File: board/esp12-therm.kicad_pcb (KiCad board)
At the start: 2 copper layers, 35.8 x 27.7 mm, 21 parts, among them J1 BATT, J2 I2C, J4 1W, Q1 IRLML6401, U1 TP4056_board, U2 ESP-12E

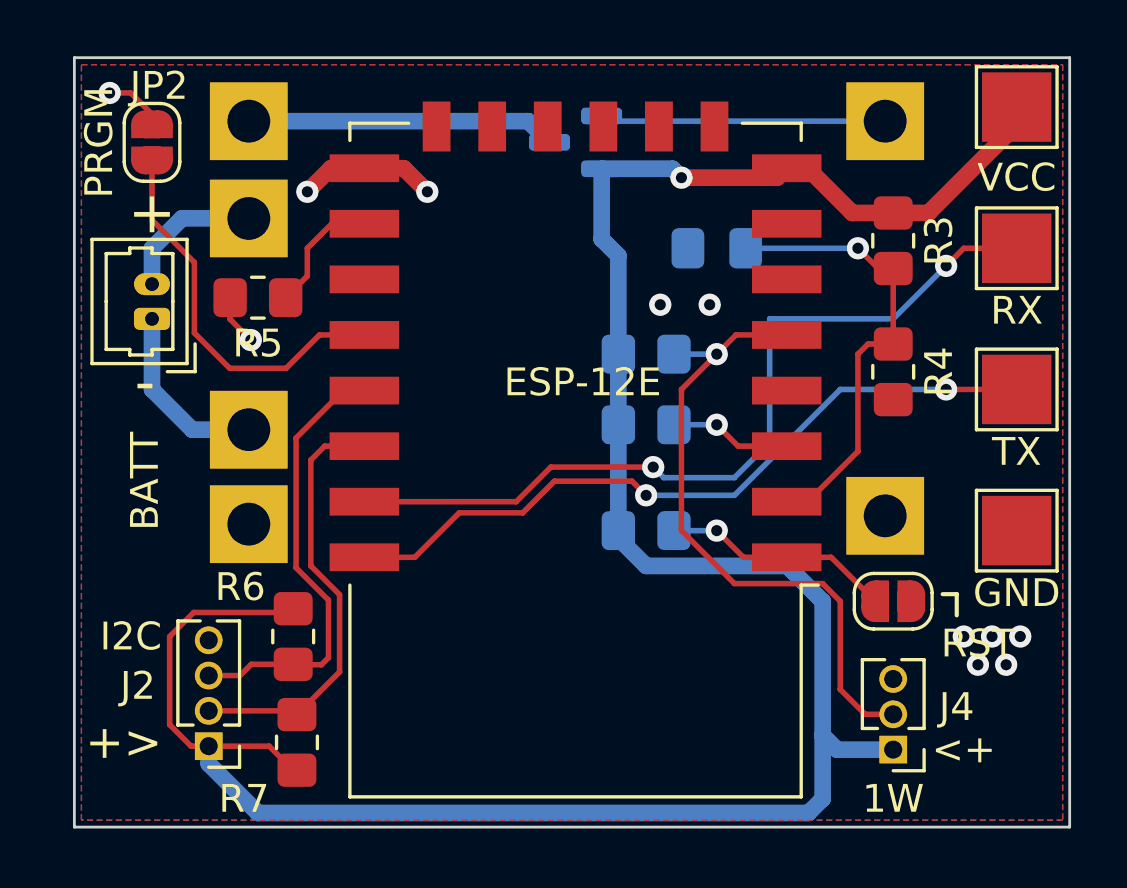
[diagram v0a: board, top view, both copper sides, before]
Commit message: Add JLC labels and silkscreen update, make board round
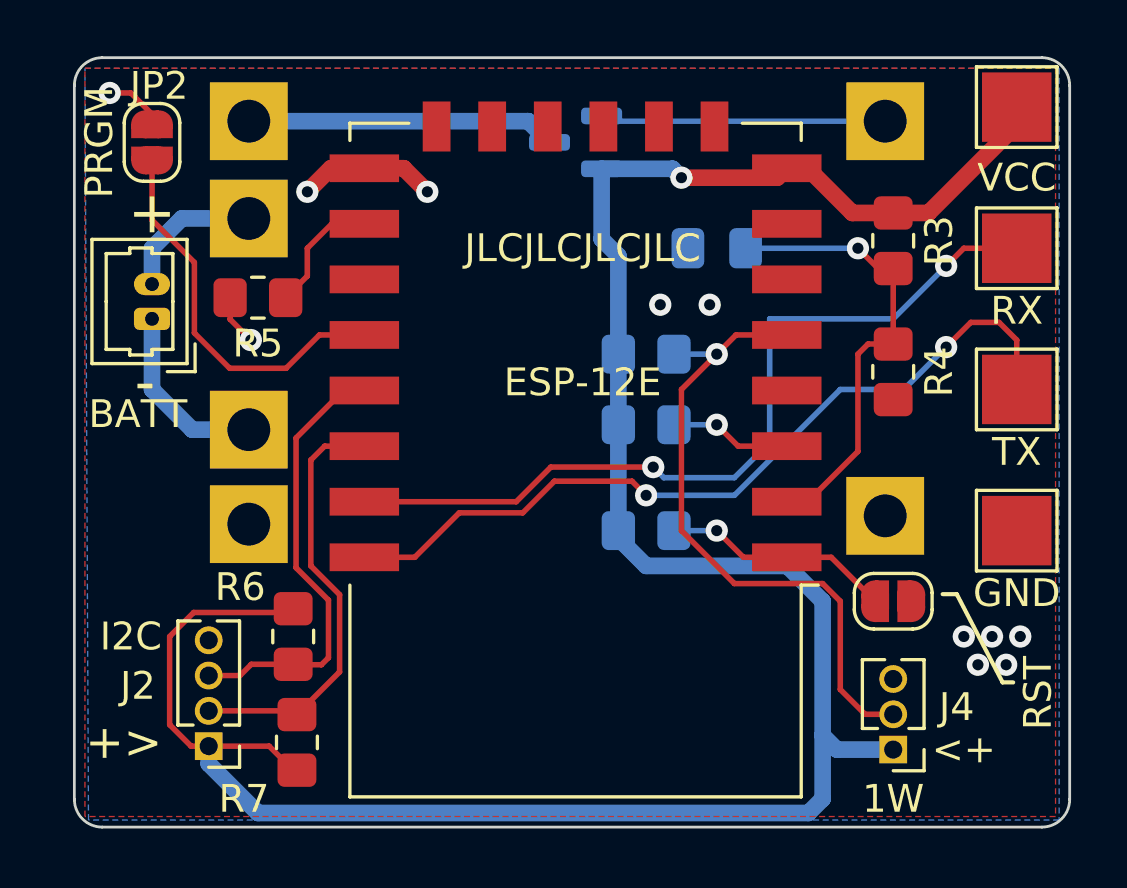
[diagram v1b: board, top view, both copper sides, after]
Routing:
- net TXD: track 26.4 -> 30.6 mm
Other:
- outline, holes or cut-outs redrawn
- board text added: "ESP12-thermometer (c) 2023"
- board text added: "JLCJLCJLCJLC"
- board text added: "https://gitlab.com/anphi/esp12-thermometer"

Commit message: Add Voltage regulator to board
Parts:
- added C2: 1u, Capacitor_SMD:C_0805_2012Metric_Pad1.18x1.45mm_HandSolder, B.Cu at (111.3, 59.2)
- added C3: 1u, Capacitor_SMD:C_0805_2012Metric_Pad1.18x1.45mm_HandSolder, B.Cu at (114.7, 60.1)
- added U3: TLV75533PDBV, Package_TO_SOT_SMD:SOT-23-5, B.Cu at (113.7, 56.3)
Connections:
- Q1 pad 2: VCC -> /VIN
- R3 pad 1: VCC -> /VIN
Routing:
- net /VIN: track 0.00 -> 37.0 mm, vias 0 -> 1
- net VCC: track 86.6 -> 90.3 mm
- net GND: track 9.06 -> 10.8 mm, vias 11 -> 10
- net RXD: track 30.2 -> 28.7 mm

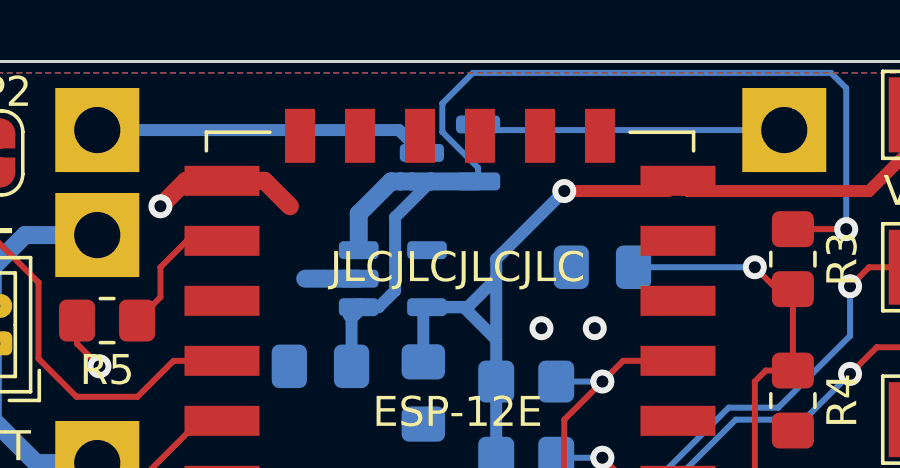
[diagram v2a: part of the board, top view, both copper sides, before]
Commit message: Change input MOSFET to an available one
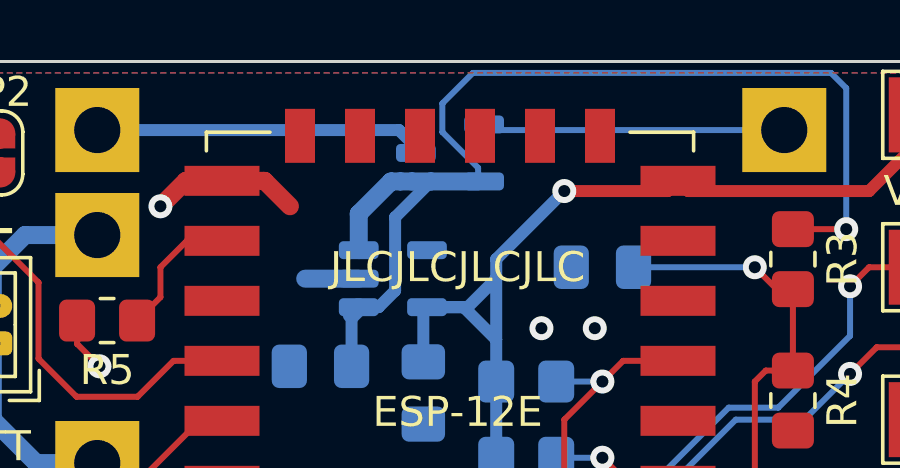
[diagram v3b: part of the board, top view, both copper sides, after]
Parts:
- Q1: value IRLML6401 -> PMF170XP; footprint Package_TO_SOT_SMD:SOT-23 -> Package_TO_SOT_SMD:SOT-23-3
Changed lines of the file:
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@@
       (net 3 "Net-(J1-Pin_1)") (pinfunction "B-") (pintype "power_out"))
   )
-  (footprint "Package_TO_SOT_SMD:SOT-23" (layer "B.Cu")
+  (footprint "Package_TO_SOT_SMD:SOT-23-3" (layer "B.Cu")
     (at 115.57 52.07 180)
-    (descr "SOT, 3 Pin (https://www.jedec.org/system/files/docs/to-236h.pdf variant AB), generated with kicad-footprint-generator ipc_gullwing_generator.py")
+    (descr "SOT, 3 Pin (https://www.jedec.org/sites/default/files/docs/Mo-178D.PDF inferred 3-pin variant), generated with kicad-footprint-generator ipc_gullwing_generator.py")
     (tags "SOT TO_SOT_SMD")
     (property "Sheetfile" "esp12-therm.kicad_sch")
@@
     (property "ki_keywords" "P-Channel HEXFET MOSFET Logic-Level")
     (attr smd)
-    (fp_text reference "Q1" (at 0 2.4) (layer "B.Fab")
+    (fp_text reference "Q1" (at 0 2.4) (layer "B.SilkS")
         (effects (font (size 1 1) (thickness 0.15)) (justify mirror))
     )
-    (fp_text value "IRLML6401" (at 0 -2.4) (layer "B.Fab")
+    (fp_text value "PMF170XP" (at 0 -2.4) (layer "B.Fab")
         (effects (font (size 1 1) (thickness 0.15)) (justify mirror))
     )
     (fp_text user "${REFERENCE}" (at 0 0) (layer "B.Fab")
-        (effects (font (size 0.32 0.32) (thickness 0.05)) (justify mirror))
+        (effects (font (size 0.4 0.4) (thickness 0.06)) (justify mirror))
     )
-    (fp_line (start 0 -1.56) (end -0.65 -1.56)
+    (fp_line (start 0 -1.56) (end -0.8 -1.56)
       (stroke (width 0.12) (type solid)) (layer "B.SilkS"))
-    (fp_line (start 0 -1.56) (end 0.65 -1.56)
+    (fp_line (start 0 -1.56) (end 0.8 -1.56)
       (stroke (width 0.12) (type solid)) (layer "B.SilkS"))
-    (fp_line (start 0 1.56) (end -1.675 1.56)
+    (fp_line (start 0 1.56) (end -1.8 1.56)
       (stroke (width 0.12) (type solid)) (layer "B.SilkS"))
-    (fp_line (start 0 1.56) (end 0.65 1.56)
+    (fp_line (start 0 1.56) (end 0.8 1.56)
       (stroke (width 0.12) (type solid)) (layer "B.SilkS"))
-    (fp_line (start -1.92 -1.7) (end 1.92 -1.7)
+    (fp_line (start -2.05 -1.7) (end 2.05 -1.7)
       (stroke (width 0.05) (type solid)) (layer "B.CrtYd"))
-    (fp_line (start -1.92 1.7) (end -1.92 -1.7)
+    (fp_line (start -2.05 1.7) (end -2.05 -1.7)
       (stroke (width 0.05) (type solid)) (layer "B.CrtYd"))
-    (fp_line (start 1.92 -1.7) (end 1.92 1.7)
+    (fp_line (start 2.05 -1.7) (end 2.05 1.7)
       (stroke (width 0.05) (type solid)) (layer "B.CrtYd"))
-    (fp_line (start 1.92 1.7) (end -1.92 1.7)
+    (fp_line (start 2.05 1.7) (end -2.05 1.7)
       (stroke (width 0.05) (type solid)) (layer "B.CrtYd"))
-    (fp_line (start -0.65 -1.45) (end -0.65 1.125)
+    (fp_line (start -0.8 -1.45) (end -0.8 1.05)
       (stroke (width 0.1) (type solid)) (layer "B.Fab"))
-    (fp_line (start -0.65 1.125) (end -0.325 1.45)
+    (fp_line (start -0.8 1.05) (end -0.4 1.45)
       (stroke (width 0.1) (type solid)) (layer "B.Fab"))
-    (fp_line (start -0.325 1.45) (end 0.65 1.45)
+    (fp_line (start -0.4 1.45) (end 0.8 1.45)
       (stroke (width 0.1) (type solid)) (layer "B.Fab"))
-    (fp_line (start 0.65 -1.45) (end -0.65 -1.45)
+    (fp_line (start 0.8 -1.45) (end -0.8 -1.45)
       (stroke (width 0.1) (type solid)) (layer "B.Fab"))
-    (fp_line (start 0.65 1.45) (end 0.65 -1.45)
+    (fp_line (start 0.8 1.45) (end 0.8 -1.45)
       (stroke (width 0.1) (type solid)) (layer "B.Fab"))
-    (pad "1" smd roundrect (at -0.9375 0.95 180) (size 1.475 0.6) (layers "B.Cu" "B.Paste" "B.Mask") (roundrect_rratio 0.25)
+    (pad "1" smd roundrect (at -1.1375 0.95 180) (size 1.325 0.6) (layers "B.Cu" "B.Paste" "B.Mask") (roundrect_rratio 0.25)
       (net 11 "Net-(Q1-G)") (pinfunction "G") (pintype "input"))
-    (pad "2" smd roundrect (at -0.9375 -0.95 180) (size 1.475 0.6) (layers "B.Cu" "B.Paste" "B.Mask") (roundrect_rratio 0.25)
+    (pad "2" smd roundrect (at -1.1375 -0.95 180) (size 1.325 0.6) (layers "B.Cu" "B.Paste" "B.Mask") (roundrect_rratio 0.25)
       (net 29 "/VIN") (pinfunction "S") (pintype "passive"))
-    (pad "3" smd roundrect (at 0.9375 0 180) (size 1.475 0.6) (layers "B.Cu" "B.Paste" "B.Mask") (roundrect_rratio 0.25)
+    (pad "3" smd roundrect (at 1.1375 0 180) (size 1.325 0.6) (layers "B.Cu" "B.Paste" "B.Mask") (roundrect_rratio 0.25)
       (net 12 "Net-(Q1-D)") (pinfunction "D") (pintype "passive"))
-    (model "${KICAD6_3DMODEL_DIR}/Package_TO_SOT_SMD.3dshapes/SOT-23.wrl"
+    (model "${KICAD6_3DMODEL_DIR}/Package_TO_SOT_SMD.3dshapes/SOT-23-3.wrl"
       (offset (xyz 0 0 0))
       (scale (xyz 1 1 1))

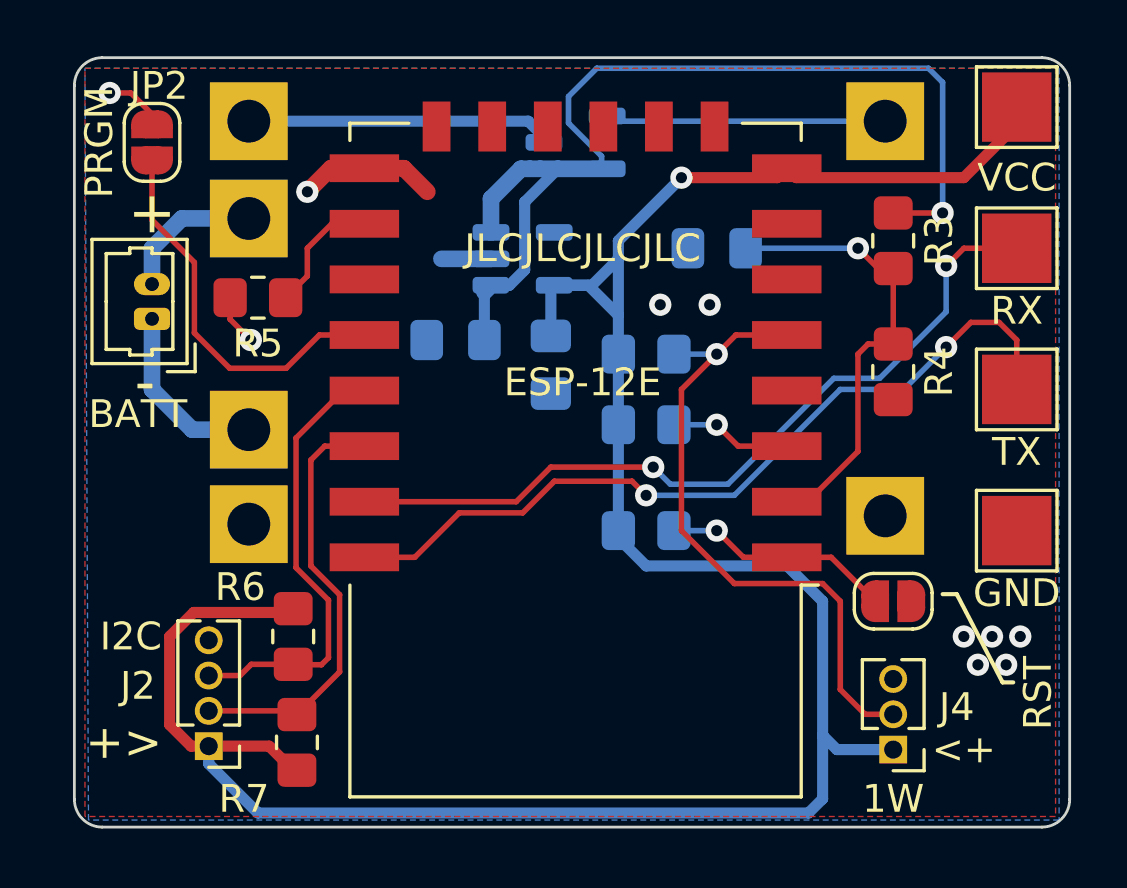
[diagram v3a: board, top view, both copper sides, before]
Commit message: * Adapt footprints to new MOSFET * Place battery bypass solder jumper
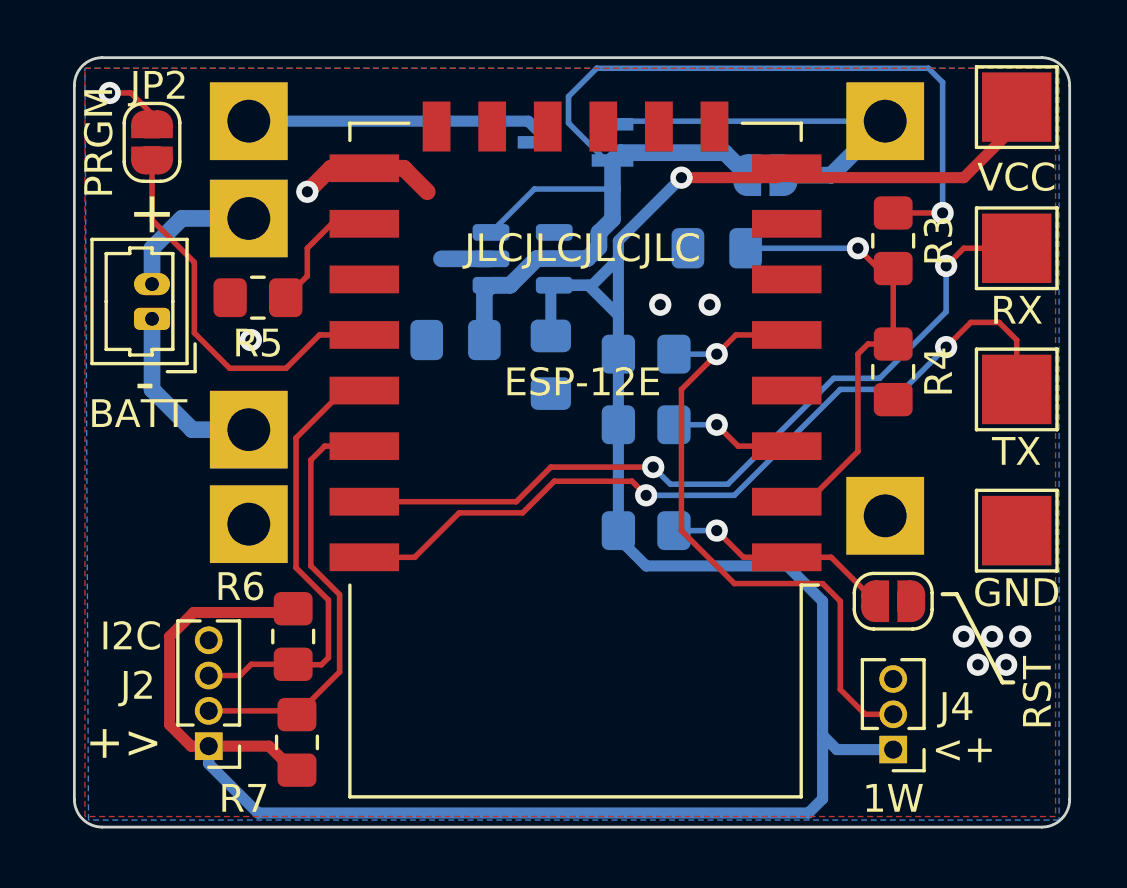
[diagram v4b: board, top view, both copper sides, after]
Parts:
- added JP3: no battery bridge, Jumper:SolderJumper-2_P1.3mm_Open_RoundedPad1.0x1.5mm, B.Cu at (122.4, 53.2)
- Q1: footprint Package_TO_SOT_SMD:SOT-23-3 -> Package_TO_SOT_SMD:SOT-323_SC-70_Handsoldering
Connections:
- U1 pad 2: unconnected-(U1-VIN--Pad2) -> GND
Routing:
- net /VIN: track 37.0 -> 43.4 mm
- net Net-(JP3-A): track 10.3 -> 14.5 mm
- net GND: track 10.8 -> 9.01 mm
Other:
- board text added: "bridge if you don't use a battery"
